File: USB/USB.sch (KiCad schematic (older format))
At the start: 30 parts, among them J1 Conn_02x12_Odd_Even, J2 Conn_02x06_Odd_Even

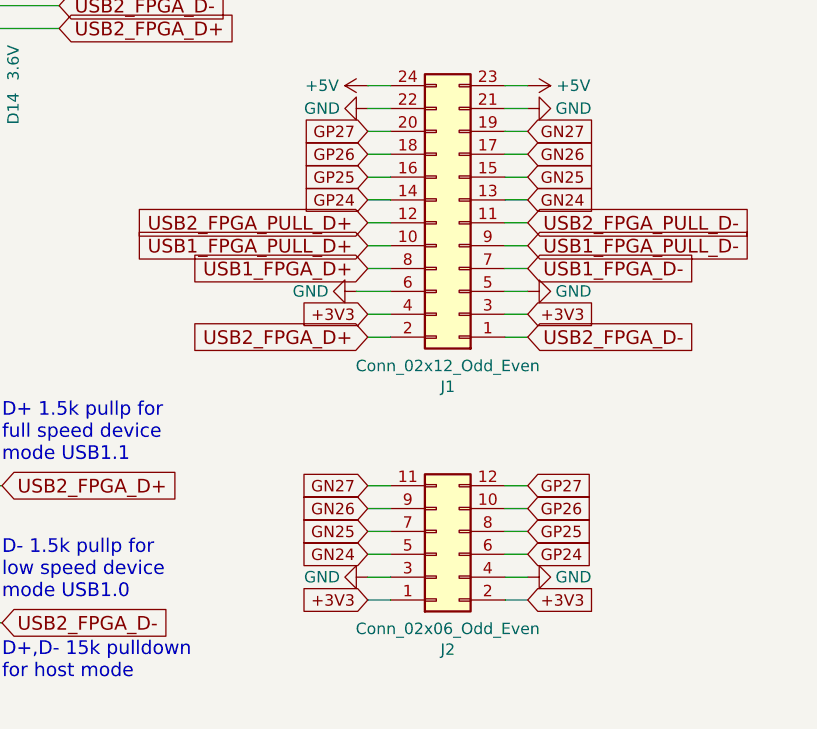
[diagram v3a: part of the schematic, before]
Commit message: Adding two missing pins
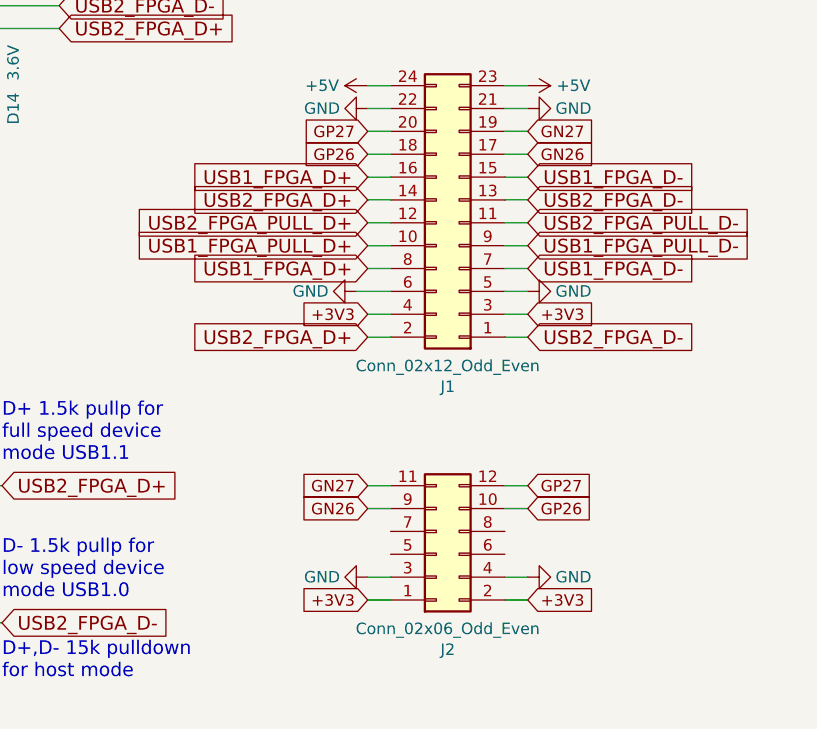
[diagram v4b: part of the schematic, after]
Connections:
- net USB1_FPGA_D+: now also J1.16 (Pin_16)
- net USB1_FPGA_D-: now also J1.15 (Pin_15)
- net USB2_FPGA_D+: now also J1.14 (Pin_14)
- net USB2_FPGA_D-: now also J1.13 (Pin_13)
- net GN24: no longer names the net of J2.5 (Pin_5)
- net GN24: no longer J1.13 (Pin_13)
- net GN25: no longer names the net of J2.7 (Pin_7)
- net GN25: no longer J1.15 (Pin_15)
- net GP24: no longer names the net of J2.6 (Pin_6)
- net GP24: no longer J1.14 (Pin_14)
- net GP25: no longer names the net of J2.8 (Pin_8)
- net GP25: no longer J1.16 (Pin_16)
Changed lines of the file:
@@
 EESchema Schematic File Version 4
-EELAYER 30 0
+LIBS:USB-cache
+EELAYER 26 0
 EELAYER END
 $Descr A4 11693 8268
@@
 Text GLabel 9750 2750 2    50   Input ~ 0
 GN26
-Text GLabel 9750 2850 2    50   Input ~ 0
-GN25
-Text GLabel 9750 2950 2    50   Input ~ 0
-GN24
 Text GLabel 9750 3450 2    50   Input ~ 0
 +3V3
@@
 Text GLabel 9050 2750 0    50   Input ~ 0
 GP26
-Text GLabel 9050 2850 0    50   Input ~ 0
-GP25
-Text GLabel 9050 2950 0    50   Input ~ 0
-GP24
 Text GLabel 9050 3450 0    50   Input ~ 0
 +3V3
@@
 Text GLabel 9050 4300 0    50   Input ~ 0
 GN26
-Text GLabel 9050 4400 0    50   Input ~ 0
-GN25
-Text GLabel 9050 4500 0    50   Input ~ 0
-GN24
 Text GLabel 9750 4200 2    50   Input ~ 0
 GP27
 Text GLabel 9750 4300 2    50   Input ~ 0
 GP26
-Text GLabel 9750 4400 2    50   Input ~ 0
-GP25
-Text GLabel 9750 4500 2    50   Input ~ 0
-GP24
 Wire Wire Line
 	9050 4200 9150 4200
@@
 	9050 4300 9150 4300
 Wire Wire Line
-	9050 4400 9150 4400
-Wire Wire Line
-	9050 4500 9150 4500
-Wire Wire Line
 	9050 4600 9150 4600
 Wire Wire Line
@@
 	9650 4300 9750 4300
 Wire Wire Line
-	9650 4400 9750 4400
-Wire Wire Line
-	9650 4500 9750 4500
-Wire Wire Line
 	9650 4600 9750 4600
 Wire Wire Line
@@
 Wire Wire Line
 	2600 2000 3450 2000
+Text GLabel 9050 2950 0    60   Input ~ 0
+USB2_FPGA_D+
+Text GLabel 9750 2950 2    60   Input ~ 0
+USB2_FPGA_D-
+Text GLabel 9750 2850 2    60   Input ~ 0
+USB1_FPGA_D-
+Text GLabel 9050 2850 0    60   Input ~ 0
+USB1_FPGA_D+
 $EndSCHEMATC

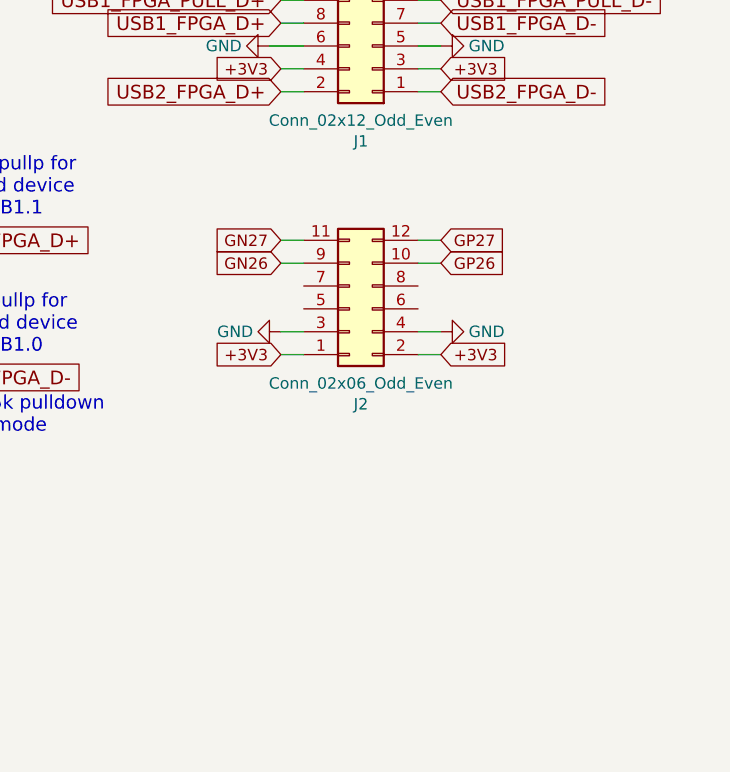
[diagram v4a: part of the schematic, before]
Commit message: Ripoff USB adding transmit receive
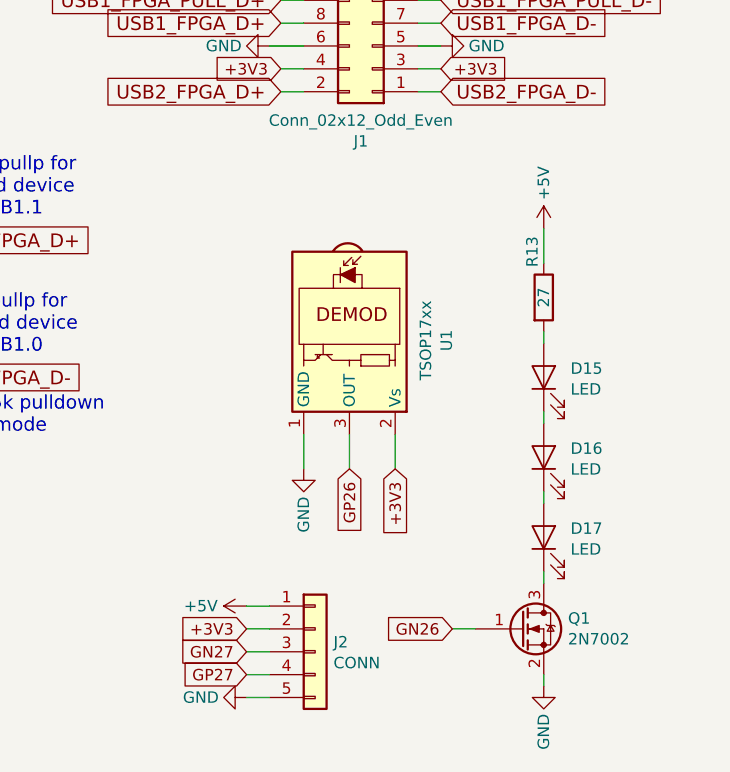
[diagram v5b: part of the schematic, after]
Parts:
- removed J2: Conn_02x06_Odd_Even, Connector_PinSocket_2.54mm:PinSocket_2x06_P2.54mm_Horizontal, symbol Connector_Generic:Conn_02x06_Odd_Even
- added D15, D16, D17: LED, LED_THT:LED_D3.0mm_IRBlack, symbol Device:LED
- added J2: CONN, Connector_PinHeader_2.54mm:PinHeader_1x05_P2.54mm_Vertical, symbol Connector_Generic:Conn_01x05
- added Q1: 2N7002, Package_TO_SOT_SMD:SOT-23, symbol Transistor_FET:2N7002
- added R13: 27, Resistor_SMD:R_0603_1608Metric, symbol Device:R
- added U1: TSOP17xx, OptoDevice:Vishay_CAST-3Pin, symbol Interface_Optical:TSOP17xx
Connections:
- net +3V3: now also J2.2 (Pin_2), U1.2 (Vs)
- net +5V: now also J2.1 (Pin_1), R13.1
- net GN26: now also Q1.1 (G)
- net GN27: now also J2.3 (Pin_3)
- net GND: now also J2.5 (Pin_5), Q1.2 (S), U1.1 (GND)
- net GP26: now also U1.3 (OUT)
- net GP27: now also J2.4 (Pin_4)
- new net: D15.1 (K), D16.2 (A)
- new net: D15.2 (A), R13.2
- new net: D16.1 (K), D17.2 (A)
- new net: D17.1 (K), Q1.3 (D)
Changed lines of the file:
@@
 EESchema Schematic File Version 4
 LIBS:USB-cache
-EELAYER 26 0
+EELAYER 30 0
 EELAYER END
 $Descr A4 11693 8268
@@
 Wire Wire Line
 	9050 3550 9150 3550
-Text GLabel 9750 4700 2    50   Input ~ 0
-+3V3
-$Comp
-L power:GND #PWR016
-U 1 1 5DFAC12F
-P 9750 4600
-F 0 "#PWR016" H 9750 4350 50  0001 C CNN
-F 1 "GND" V 9750 4400 50  0000 C CNN
-F 2 "" H 9750 4600 50  0001 C CNN
-F 3 "" H 9750 4600 50  0001 C CNN
-	1    9750 4600
-	0    -1   -1   0
-$EndComp
-$Comp
-L power:GND #PWR012
-U 1 1 5DFAC5A9
-P 9050 4600
-F 0 "#PWR012" H 9050 4350 50  0001 C CNN
-F 1 "GND" V 9050 4400 50  0000 C CNN
-F 2 "" H 9050 4600 50  0001 C CNN
-F 3 "" H 9050 4600 50  0001 C CNN
-	1    9050 4600
-	0    1    1    0
-$EndComp
-Text GLabel 9050 4700 0    50   Input ~ 0
-+3V3
-Text GLabel 9050 4200 0    50   Input ~ 0
-GN27
-Text GLabel 9050 4300 0    50   Input ~ 0
-GN26
-Text GLabel 9750 4200 2    50   Input ~ 0
-GP27
-Text GLabel 9750 4300 2    50   Input ~ 0
+Text GLabel 9350 5200 3    50   Input ~ 0
 GP26
-Wire Wire Line
-	9050 4200 9150 4200
-Wire Wire Line
-	9650 4200 9750 4200
-Wire Wire Line
-	9050 4300 9150 4300
-Wire Wire Line
-	9050 4600 9150 4600
-Wire Wire Line
-	9050 4700 9150 4700
-Wire Wire Line
-	9650 4300 9750 4300
-Wire Wire Line
-	9650 4600 9750 4600
-Wire Wire Line
-	9650 4700 9750 4700
 Text GLabel 9750 3250 2    60   Input ~ 0
 USB1_FPGA_D-
@@
 USB2_FPGA_PULL_D-
 $Comp
-L Connector_Generic:Conn_02x06_Odd_Even J2
-U 1 1 5DFAA8B3
-P 9350 4500
-F 0 "J2" H 9400 4917 50  0000 C CNN
-F 1 "Conn_02x06_Odd_Even" H 9400 4826 50  0000 C CNN
-F 2 "Connector_PinSocket_2.54mm:PinSocket_2x06_P2.54mm_Horizontal" H 9350 4500 50  0001 C CNN
-F 3 "~" H 9350 4500 50  0001 C CNN
-	1    9350 4500
-	1    0    0    1
-$EndComp
-$Comp
 L Connector:USB_A US4
 U 1 1 5DF9BA2D
@@
 Text GLabel 9050 2850 0    60   Input ~ 0
 USB1_FPGA_D+
+$Comp
+L Interface_Optical:TSOP17xx U1
+U 1 1 5E048AE5
+P 9350 4650
+F 0 "U1" H 9338 5075 50  0000 C CNN
+F 1 "TSOP17xx" H 9338 4984 50  0000 C CNN
+F 2 "OptoDevice:Vishay_CAST-3Pin" H 9300 4275 50  0001 C CNN
+F 3 "http://www.micropik.com/PDF/tsop17xx.pdf" H 10000 4950 50  0001 C CNN
+	1    9350 4650
+	0    1    1    0
+$EndComp
+Text GLabel 9550 5200 3    50   Input ~ 0
++3V3
+$Comp
+L power:GND #PWR02
+U 1 1 5E04A1C0
+P 9150 5200
+F 0 "#PWR02" H 9150 4950 50  0001 C CNN
+F 1 "GND" V 9150 5000 50  0000 C CNN
+F 2 "" H 9150 5200 50  0001 C CNN
+F 3 "" H 9150 5200 50  0001 C CNN
+	1    9150 5200
+	1    0    0    -1
+$EndComp
+Wire Wire Line
+	9350 5050 9350 5200
+Wire Wire Line
+	9550 5050 9550 5200
+Wire Wire Line
+	9150 5050 9150 5200
+$Comp
+L Device:LED D15
+U 1 1 5E05440B
+P 10200 4800
+F 0 "D15" V 10239 4683 50  0000 R CNN
+F 1 "LED" V 10148 4683 50  0000 R CNN
+F 2 "LED_THT:LED_D3.0mm_IRBlack" H 10200 4800 50  0001 C CNN
+F 3 "~" H 10200 4800 50  0001 C CNN
+	1    10200 4800
+	0    -1   -1   0
+$EndComp
+$Comp
+L Device:LED D16
+U 1 1 5E05565F
+P 10200 5150
+F 0 "D16" V 10239 5033 50  0000 R CNN
+F 1 "LED" V 10148 5033 50  0000 R CNN
+F 2 "LED_THT:LED_D3.0mm_IRBlack" H 10200 5150 50  0001 C CNN
+F 3 "~" H 10200 5150 50  0001 C CNN
+	1    10200 5150
+	0    -1   -1   0
+$EndComp
+$Comp
+L Device:LED D17
+U 1 1 5E05591A
+P 10200 5500
+F 0 "D17" V 10239 5383 50  0000 R CNN
+F 1 "LED" V 10148 5383 50  0000 R CNN
+F 2 "LED_THT:LED_D3.0mm_IRBlack" H 10200 5500 50  0001 C CNN
+F 3 "~" H 10200 5500 50  0001 C CNN
+	1    10200 5500
+	0    -1   -1   0
+$EndComp
+$Comp
+L Device:R R13
+U 1 1 5E055BA4
+P 10200 4450
+AR Path="/5E055BA4" Ref="R13"  Part="1"
+AR Path="/58D6BF46/5E055BA4" Ref="R?"  Part="1"
+F 0 "R13" V 10150 4650 50  0000 C CNN
+F 1 "27" V 10200 4450 50  0000 C CNN
+F 2 "Resistor_SMD:R_0603_1608Metric" V 10130 4450 50  0001 C CNN
+F 3 "" H 10200 4450 50  0000 C CNN
+F 4 "www.yageo.com" V 10200 4450 50  0001 C CNN "MNF1_URL"
+F 5 "AC0603JR-0727RL" V 10200 4450 50  0001 C CNN "MPN"
+	1    10200 4450
+	1    0    0    -1
+$EndComp
+$Comp
+L Transistor_FET:2N7002 Q1
+U 1 1 5E0572AC
+P 10100 5900
+F 0 "Q1" H 10306 5946 50  0000 L CNN
+F 1 "2N7002" H 10306 5855 50  0000 L CNN
+F 2 "Package_TO_SOT_SMD:SOT-23" H 10300 5825 50  0001 L CIN
+F 3 "https://www.fairchildsemi.com/datasheets/2N/2N7002.pdf" H 10100 5900 50  0001 L CNN
+	1    10100 5900
+	1    0    0    -1
+$EndComp
+$Comp
+L power:GND #PWR012
+U 1 1 5E059E1E
+P 10200 6150
+F 0 "#PWR012" H 10200 5900 50  0001 C CNN
+F 1 "GND" V 10200 5950 50  0000 C CNN
+F 2 "" H 10200 6150 50  0001 C CNN
+F 3 "" H 10200 6150 50  0001 C CNN
+	1    10200 6150
+	1    0    0    -1
+$EndComp
+$Comp
+L power:+5V #PWR06
+U 1 1 5E05A4D5
+P 10200 4150
+F 0 "#PWR06" H 10200 4000 50  0001 C CNN
+F 1 "+5V" V 10200 4350 50  0000 C CNN
+F 2 "" H 10200 4150 60  0000 C CNN
+F 3 "" H 10200 4150 60  0000 C CNN
+	1    10200 4150
+	1    0    0    -1
+$EndComp
+Wire Wire Line
+	10200 4150 10200 4300
+Wire Wire Line
+	10200 4600 10200 4650
+Wire Wire Line
+	10200 4950 10200 5000
+Wire Wire Line
+	10200 5300 10200 5350
+Wire Wire Line
+	10200 5650 10200 5700
+Wire Wire Line
+	10200 6100 10200 6150
+Text GLabel 9800 5900 0    50   Input ~ 0
+GN26
+Wire Wire Line
+	9800 5900 9900 5900
+$Comp
+L Connector_Generic:Conn_01x05 J2
+U 1 1 5E07EEC9
+P 9200 6000
+F 0 "J2" H 9280 6042 50  0000 L CNN
+F 1 "CONN" H 9280 5951 50  0000 L CNN
+F 2 "Connector_PinHeader_2.54mm:PinHeader_1x05_P2.54mm_Vertical" H 9200 6000 50  0001 C CNN
+F 3 "~" H 9200 6000 50  0001 C CNN
+	1    9200 6000
+	1    0    0    -1
+$EndComp
+$Comp
+L power:+5V #PWR016
+U 1 1 5E07F755
+P 8900 5800
+F 0 "#PWR016" H 8900 5650 50  0001 C CNN
+F 1 "+5V" V 8900 6000 50  0000 C CNN
+F 2 "" H 8900 5800 60  0000 C CNN
+F 3 "" H 8900 5800 60  0000 C CNN
+	1    8900 5800
+	0    -1   -1   0
+$EndComp
+Text GLabel 8900 6100 0    50   Input ~ 0
+GP27
+Text GLabel 8900 6000 0    50   Input ~ 0
+GN27
+Text GLabel 8900 5900 0    50   Input ~ 0
++3V3
+$Comp
+L power:GND #PWR017
+U 1 1 5E07FF1E
+P 8900 6200
+F 0 "#PWR017" H 8900 5950 50  0001 C CNN
+F 1 "GND" V 8900 6000 50  0000 C CNN
+F 2 "" H 8900 6200 50  0001 C CNN
+F 3 "" H 8900 6200 50  0001 C CNN
+	1    8900 6200
+	0    1    1    0
+$EndComp
+Wire Wire Line
+	8900 5800 9000 5800
+Wire Wire Line
+	8900 5900 9000 5900
+Wire Wire Line
+	8900 6000 9000 6000
+Wire Wire Line
+	8900 6100 9000 6100
+Wire Wire Line
+	8900 6200 9000 6200
 $EndSCHEMATC

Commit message: Adding new routed PCB
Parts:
- R13: value 27 -> 4.7
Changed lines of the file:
@@
 EESchema Schematic File Version 4
 LIBS:USB-cache
-EELAYER 30 0
+EELAYER 26 0
 EELAYER END
 $Descr A4 11693 8268
@@
 AR Path="/58D6BF46/5E055BA4" Ref="R?"  Part="1"
 F 0 "R13" V 10150 4650 50  0000 C CNN
-F 1 "27" V 10200 4450 50  0000 C CNN
+F 1 "4.7" V 10200 4450 50  0000 C CNN
 F 2 "Resistor_SMD:R_0603_1608Metric" V 10130 4450 50  0001 C CNN
 F 3 "" H 10200 4450 50  0000 C CNN

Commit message: Shematics update
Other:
- note added: "D5,D7: Schottky 2A/30V \nLow drop Vfmax=0.375V\nParts reduction: Only D5 is required.\nD6, D13 can be 1206\n1A polyfuses or 0-ohm/2A jumpers"
- note added: "Deviation from USB specification in\npulldowns for BOM simplificaton.\nWith series diode, correct value R2 R4 \nshould be 12k but 15k is used."
- note removed: "D8,D9: Schottky 2A/30V \nLow drop Vfmax=0.375V\nParts reduction: Only D8 is required.\nD9 D51 D52 can be 1206\n1A polyfuses or 0-ohm/2A jumpers"
- note removed: "Deviation from USB specification in\npulldowns for BOM simplificaton.\nWith series diode, correct value R63 R64 \nshould be 12k but 15k is used."
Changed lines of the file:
@@
 EESchema Schematic File Version 4
-LIBS:USB-cache
-EELAYER 26 0
+EELAYER 30 0
 EELAYER END
 $Descr A4 11693 8268
 encoding utf-8
 Sheet 1 1
-Title ""
-Date ""
-Rev ""
-Comp ""
+Title "ULX3S USB PMOD"
+Date "2020-10-08"
+Rev "V1.0"
+Comp "Radiona.org"
 Comment1 ""
 Comment2 ""
@@
 Connection ~ 3600 2100
 Text Notes 1550 3450 0    60   ~ 0
-D8,D9: Schottky 2A/30V \nLow drop Vfmax=0.375V\nParts reduction: Only D8 is required.\nD9 D51 D52 can be 1206\n1A polyfuses or 0-ohm/2A jumpers
+D5,D7: Schottky 2A/30V \nLow drop Vfmax=0.375V\nParts reduction: Only D5 is required.\nD6, D13 can be 1206\n1A polyfuses or 0-ohm/2A jumpers
 $Comp
 L Device:R R3
@@
 US1VBUS
 Text Notes 1650 5400 0    60   ~ 0
-Deviation from USB specification in\npulldowns for BOM simplificaton.\nWith series diode, correct value R63 R64 \nshould be 12k but 15k is used.
+Deviation from USB specification in\npulldowns for BOM simplificaton.\nWith series diode, correct value R2 R4 \nshould be 12k but 15k is used.
 Wire Notes Line
 	3450 1750 3550 1750
